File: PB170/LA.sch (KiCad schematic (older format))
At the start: 0 parts

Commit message: 11-02-2021 02 Martin
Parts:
- added U? (x3): 74HC08, Housings_SOIC:SOIC-14_3.9x8.7mm_Pitch1.27mm, symbol PB170:74HC08
- added U? (x3): 74HC32, Housings_SOIC:SOIC-14_3.9x8.7mm_Pitch1.27mm, symbol PB170:74HC32
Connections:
- new net: U?.3 (1Y), U?.4 (2A)
- new net: U?.3 (1Y), U?.9 (3A)
- new net: U?.5 (2B), U?.6 (2Y)
- new net: U?.10 (3B), U?.8 (3Y)
- new net: U?.6 (2Y), U?.9 (3A)
- new net LA: U?.8 (3Y)
- new net Q0: U?.1 (1A)
- new net Q2: U?.4 (2A)
- new net Q3: U?.1 (1A)
- new net Q4: U?.2 (1B)
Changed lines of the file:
@@
 Comment4 ""
 $EndDescr
+$Comp
+L PB170:74HC08 U?
+U 1 1 6025D3F6
+P 1450 1000
+F 0 "U?" H 1475 1267 50  0000 C CNN
+F 1 "74HC08" H 1475 1176 50  0000 C CNN
+F 2 "Housings_SOIC:SOIC-14_3.9x8.7mm_Pitch1.27mm" H 1450 1000 50  0001 C CNN
+F 3 "https://datasheet.lcsc.com/szlcsc/Nexperia-74HC08D-653_C5593.pdf" H 1450 1000 50  0001 C CNN
+F 4 "C5593" H 1450 1000 50  0001 C CNN "LCSC"
+	1    1450 1000
+	1    0    0    -1
+$EndComp
+$Comp
+L PB170:74HC08 U?
+U 2 1 6025D87D
+P 1450 1500
+F 0 "U?" H 1475 1767 50  0000 C CNN
+F 1 "74HC08" H 1475 1676 50  0000 C CNN
+F 2 "Housings_SOIC:SOIC-14_3.9x8.7mm_Pitch1.27mm" H 1450 1500 50  0001 C CNN
+F 3 "https://datasheet.lcsc.com/szlcsc/Nexperia-74HC08D-653_C5593.pdf" H 1450 1500 50  0001 C CNN
+F 4 "C5593" H 1450 1500 50  0001 C CNN "LCSC"
+	2    1450 1500
+	1    0    0    -1
+$EndComp
+$Comp
+L PB170:74HC08 U?
+U 3 1 6025DDC8
+P 2400 1950
+F 0 "U?" H 2425 2217 50  0000 C CNN
+F 1 "74HC08" H 2425 2126 50  0000 C CNN
+F 2 "Housings_SOIC:SOIC-14_3.9x8.7mm_Pitch1.27mm" H 2400 1950 50  0001 C CNN
+F 3 "https://datasheet.lcsc.com/szlcsc/Nexperia-74HC08D-653_C5593.pdf" H 2400 1950 50  0001 C CNN
+F 4 "C5593" H 2400 1950 50  0001 C CNN "LCSC"
+	3    2400 1950
+	1    0    0    -1
+$EndComp
+$Comp
+L PB170:74HC32 U?
+U 1 1 6025D4D4
+P 1500 1900
+F 0 "U?" H 1475 2175 50  0000 C CNN
+F 1 "74HC32" H 1475 2084 50  0000 C CNN
+F 2 "Housings_SOIC:SOIC-14_3.9x8.7mm_Pitch1.27mm" H 950 2100 50  0001 C CNN
+F 3 "https://datasheet.lcsc.com/szlcsc/Nexperia-74HC32D-653_C5632.pdf" H 950 2100 50  0001 C CNN
+F 4 "C5632" H 1500 1900 50  0001 C CNN "LCSC"
+	1    1500 1900
+	1    0    0    -1
+$EndComp
+$Comp
+L PB170:74HC32 U?
+U 2 1 6025E621
+P 2450 1200
+F 0 "U?" H 2425 1475 50  0000 C CNN
+F 1 "74HC32" H 2425 1384 50  0000 C CNN
+F 2 "Housings_SOIC:SOIC-14_3.9x8.7mm_Pitch1.27mm" H 1900 1400 50  0001 C CNN
+F 3 "https://datasheet.lcsc.com/szlcsc/Nexperia-74HC32D-653_C5632.pdf" H 1900 1400 50  0001 C CNN
+F 4 "C5632" H 2450 1200 50  0001 C CNN "LCSC"
+	2    2450 1200
+	1    0    0    -1
+$EndComp
+$Comp
+L PB170:74HC32 U?
+U 3 1 6025FAD0
+P 3050 1500
+F 0 "U?" H 3025 1775 50  0000 C CNN
+F 1 "74HC32" H 3025 1684 50  0000 C CNN
+F 2 "Housings_SOIC:SOIC-14_3.9x8.7mm_Pitch1.27mm" H 2500 1700 50  0001 C CNN
+F 3 "https://datasheet.lcsc.com/szlcsc/Nexperia-74HC32D-653_C5632.pdf" H 2500 1700 50  0001 C CNN
+F 4 "C5632" H 3050 1500 50  0001 C CNN "LCSC"
+	3    3050 1500
+	1    0    0    -1
+$EndComp
+Wire Wire Line
+	1750 1000 2050 1000
+Wire Wire Line
+	2050 1000 2050 1150
+Wire Wire Line
+	2050 1150 2200 1150
+Wire Wire Line
+	1750 1500 2050 1500
+Wire Wire Line
+	2050 1500 2050 1250
+Wire Wire Line
+	2050 1250 2200 1250
+Wire Wire Line
+	1700 1900 2150 1900
+Wire Wire Line
+	2700 1950 2750 1950
+Wire Wire Line
+	2750 1950 2750 1550
+Wire Wire Line
+	2750 1550 2800 1550
+Wire Wire Line
+	2800 1450 2750 1450
+Wire Wire Line
+	2750 1450 2750 1200
+Wire Wire Line
+	2750 1200 2650 1200
+Text GLabel 1200 950  0    50   Input ~ 0
+Q0
+Text GLabel 1250 1850 0    50   Input ~ 0
+Q3
+Text GLabel 1200 1450 0    50   Input ~ 0
+Q2
+Text GLabel 1250 1950 0    50   Input ~ 0
+Q4
+Text GLabel 3250 1500 2    50   Output ~ 0
+LA
 $EndSCHEMATC

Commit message: LA changed
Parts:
- added U?: 74HC00, Package_SO:TSSOP-14_4.4x5mm_P0.65mm, symbol 74xx:74HC00
- U? (x2): value 74HC08 -> 74HC00; footprint Housings_SOIC:SOIC-14_3.9x8.7mm_Pitch1.27mm -> Package_SO:TSSOP-14_4.4x5mm_P0.65mm
- U? (x2): value 74HC32 -> 74HC00; footprint Housings_SOIC:SOIC-14_3.9x8.7mm_Pitch1.27mm -> Package_SO:TSSOP-14_4.4x5mm_P0.65mm
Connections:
- net at U?.2 (1B): now also U?.3
- net 11: now reaches U?.5 (2B)
- net 11: now also U?.1, U?.2
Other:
- moved on the sheet: U?A, U?B, U?C
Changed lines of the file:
@@
 L PB170:74HC08 U?
 U 1 1 6025D3F6
-P 1450 1000
-F 0 "U?" H 1475 1267 50  0000 C CNN
-F 1 "74HC08" H 1475 1176 50  0000 C CNN
-F 2 "Housings_SOIC:SOIC-14_3.9x8.7mm_Pitch1.27mm" H 1450 1000 50  0001 C CNN
-F 3 "https://datasheet.lcsc.com/szlcsc/Nexperia-74HC08D-653_C5593.pdf" H 1450 1000 50  0001 C CNN
-F 4 "C5593" H 1450 1000 50  0001 C CNN "LCSC"
-	1    1450 1000
+P 5200 3300
+F 0 "U?" H 5225 3567 50  0000 C CNN
+F 1 "74HC08" H 5225 3476 50  0000 C CNN
+F 2 "Housings_SOIC:SOIC-14_3.9x8.7mm_Pitch1.27mm" H 5200 3300 50  0001 C CNN
+F 3 "https://datasheet.lcsc.com/szlcsc/Nexperia-74HC08D-653_C5593.pdf" H 5200 3300 50  0001 C CNN
+F 4 "C5593" H 5200 3300 50  0001 C CNN "LCSC"
+	1    5200 3300
 	1    0    0    -1
 $EndComp
@@
 L PB170:74HC08 U?
 U 2 1 6025D87D
-P 1450 1500
-F 0 "U?" H 1475 1767 50  0000 C CNN
-F 1 "74HC08" H 1475 1676 50  0000 C CNN
-F 2 "Housings_SOIC:SOIC-14_3.9x8.7mm_Pitch1.27mm" H 1450 1500 50  0001 C CNN
-F 3 "https://datasheet.lcsc.com/szlcsc/Nexperia-74HC08D-653_C5593.pdf" H 1450 1500 50  0001 C CNN
-F 4 "C5593" H 1450 1500 50  0001 C CNN "LCSC"
-	2    1450 1500
+P 5200 3800
+F 0 "U?" H 5225 4067 50  0000 C CNN
+F 1 "74HC00" H 5225 3976 50  0000 C CNN
+F 2 "Package_SO:TSSOP-14_4.4x5mm_P0.65mm" H 5200 3800 50  0001 C CNN
+F 3 "https://datasheet.lcsc.com/szlcsc/Texas-Instruments-TI-SN74HC00PWR_C6807.pdf" H 5200 3800 50  0001 C CNN
+F 4 "C5593" H 5200 3800 50  0001 C CNN "LCSC"
+	2    5200 3800
 	1    0    0    -1
 $EndComp
@@
 L PB170:74HC08 U?
 U 3 1 6025DDC8
-P 2400 1950
-F 0 "U?" H 2425 2217 50  0000 C CNN
-F 1 "74HC08" H 2425 2126 50  0000 C CNN
-F 2 "Housings_SOIC:SOIC-14_3.9x8.7mm_Pitch1.27mm" H 2400 1950 50  0001 C CNN
-F 3 "https://datasheet.lcsc.com/szlcsc/Nexperia-74HC08D-653_C5593.pdf" H 2400 1950 50  0001 C CNN
-F 4 "C5593" H 2400 1950 50  0001 C CNN "LCSC"
-	3    2400 1950
+P 6150 4250
+F 0 "U?" H 6175 4517 50  0000 C CNN
+F 1 "74HC00" H 6175 4426 50  0000 C CNN
+F 2 "Package_SO:TSSOP-14_4.4x5mm_P0.65mm" H 6150 4250 50  0001 C CNN
+F 3 "https://datasheet.lcsc.com/szlcsc/Texas-Instruments-TI-SN74HC00PWR_C6807.pdf" H 6150 4250 50  0001 C CNN
+F 4 "C5593" H 6150 4250 50  0001 C CNN "LCSC"
+	3    6150 4250
 	1    0    0    -1
 $EndComp
@@
 L PB170:74HC32 U?
 U 1 1 6025D4D4
-P 1500 1900
-F 0 "U?" H 1475 2175 50  0000 C CNN
-F 1 "74HC32" H 1475 2084 50  0000 C CNN
-F 2 "Housings_SOIC:SOIC-14_3.9x8.7mm_Pitch1.27mm" H 950 2100 50  0001 C CNN
-F 3 "https://datasheet.lcsc.com/szlcsc/Nexperia-74HC32D-653_C5632.pdf" H 950 2100 50  0001 C CNN
-F 4 "C5632" H 1500 1900 50  0001 C CNN "LCSC"
-	1    1500 1900
+P 5250 4200
+F 0 "U?" H 5225 4475 50  0000 C CNN
+F 1 "74HC32" H 5225 4384 50  0000 C CNN
+F 2 "Housings_SOIC:SOIC-14_3.9x8.7mm_Pitch1.27mm" H 4700 4400 50  0001 C CNN
+F 3 "https://datasheet.lcsc.com/szlcsc/Nexperia-74HC32D-653_C5632.pdf" H 4700 4400 50  0001 C CNN
+F 4 "C5632" H 5250 4200 50  0001 C CNN "LCSC"
+	1    5250 4200
 	1    0    0    -1
 $EndComp
@@
 L PB170:74HC32 U?
 U 2 1 6025E621
-P 2450 1200
-F 0 "U?" H 2425 1475 50  0000 C CNN
-F 1 "74HC32" H 2425 1384 50  0000 C CNN
-F 2 "Housings_SOIC:SOIC-14_3.9x8.7mm_Pitch1.27mm" H 1900 1400 50  0001 C CNN
-F 3 "https://datasheet.lcsc.com/szlcsc/Nexperia-74HC32D-653_C5632.pdf" H 1900 1400 50  0001 C CNN
-F 4 "C5632" H 2450 1200 50  0001 C CNN "LCSC"
-	2    2450 1200
+P 6200 3500
+F 0 "U?" H 6175 3775 50  0000 C CNN
+F 1 "74HC00" H 6175 3684 50  0000 C CNN
+F 2 "Package_SO:TSSOP-14_4.4x5mm_P0.65mm" H 5650 3700 50  0001 C CNN
+F 3 "https://datasheet.lcsc.com/szlcsc/Texas-Instruments-TI-SN74HC00PWR_C6807.pdf" H 5650 3700 50  0001 C CNN
+F 4 "C5632" H 6200 3500 50  0001 C CNN "LCSC"
+	2    6200 3500
 	1    0    0    -1
 $EndComp
@@
 L PB170:74HC32 U?
 U 3 1 6025FAD0
-P 3050 1500
-F 0 "U?" H 3025 1775 50  0000 C CNN
-F 1 "74HC32" H 3025 1684 50  0000 C CNN
-F 2 "Housings_SOIC:SOIC-14_3.9x8.7mm_Pitch1.27mm" H 2500 1700 50  0001 C CNN
-F 3 "https://datasheet.lcsc.com/szlcsc/Nexperia-74HC32D-653_C5632.pdf" H 2500 1700 50  0001 C CNN
-F 4 "C5632" H 3050 1500 50  0001 C CNN "LCSC"
-	3    3050 1500
+P 6800 3800
+F 0 "U?" H 6775 4075 50  0000 C CNN
+F 1 "74HC00" H 6775 3984 50  0000 C CNN
+F 2 "Package_SO:TSSOP-14_4.4x5mm_P0.65mm" H 6250 4000 50  0001 C CNN
+F 3 "https://datasheet.lcsc.com/szlcsc/Texas-Instruments-TI-SN74HC00PWR_C6807.pdf" H 6250 4000 50  0001 C CNN
+F 4 "C5632" H 6800 3800 50  0001 C CNN "LCSC"
+	3    6800 3800
 	1    0    0    -1
 $EndComp
 Wire Wire Line
-	1750 1000 2050 1000
+	5500 3300 5800 3300
 Wire Wire Line
-	2050 1000 2050 1150
+	5800 3300 5800 3450
 Wire Wire Line
-	2050 1150 2200 1150
+	5800 3450 5950 3450
 Wire Wire Line
-	1750 1500 2050 1500
+	5500 3800 5800 3800
 Wire Wire Line
-	2050 1500 2050 1250
+	5800 3800 5800 3550
 Wire Wire Line
-	2050 1250 2200 1250
+	5800 3550 5950 3550
 Wire Wire Line
-	1700 1900 2150 1900
+	5450 4200 5900 4200
 Wire Wire Line
-	2700 1950 2750 1950
+	6450 4250 6500 4250
 Wire Wire Line
-	2750 1950 2750 1550
+	6500 4250 6500 3850
 Wire Wire Line
-	2750 1550 2800 1550
+	6500 3850 6550 3850
 Wire Wire Line
-	2800 1450 2750 1450
+	6550 3750 6500 3750
 Wire Wire Line
-	2750 1450 2750 1200
+	6500 3750 6500 3500
 Wire Wire Line
-	2750 1200 2650 1200
-Text GLabel 1200 950  0    50   Input ~ 0
+	6500 3500 6400 3500
+Text GLabel 4950 3250 0    50   Input ~ 0
 Q0
-Text GLabel 1250 1850 0    50   Input ~ 0
+Text GLabel 5000 4150 0    50   Input ~ 0
 Q3
-Text GLabel 1200 1450 0    50   Input ~ 0
+Text GLabel 4950 3750 0    50   Input ~ 0
 Q2
-Text GLabel 1250 1950 0    50   Input ~ 0
+Text GLabel 5000 4250 0    50   Input ~ 0
 Q4
-Text GLabel 3250 1500 2    50   Output ~ 0
+Text GLabel 7000 3800 2    50   Output ~ 0
 LA
+$Comp
+L 74xx:74HC00 U?
+U 1 1 6027EE26
+P 4400 3350
+F 0 "U?" H 4400 3675 50  0000 C CNN
+F 1 "74HC00" H 4400 3584 50  0000 C CNN
+F 2 "Package_SO:TSSOP-14_4.4x5mm_P0.65mm" H 4400 3350 50  0001 C CNN
+F 3 "https://datasheet.lcsc.com/szlcsc/Texas-Instruments-TI-SN74HC00PWR_C6807.pdf" H 4400 3350 50  0001 C CNN
+F 4 "C6807" H 4400 3350 50  0001 C CNN "LCSC"
+	1    4400 3350
+	1    0    0    -1
+$EndComp
+Wire Wire Line
+	4950 3350 4700 3350
+Wire Wire Line
+	4100 3250 4000 3250
+Wire Wire Line
+	4000 3250 4000 3350
+Wire Wire Line
+	4000 3450 4100 3450
+Wire Wire Line
+	4000 3350 3900 3350
+Connection ~ 4000 3350
+Wire Wire Line
+	4000 3350 4000 3450
+Text GLabel 3900 3350 0    50   Input ~ 0
+11
+Wire Wire Line
+	4000 3450 4000 3850
+Wire Wire Line
+	4000 3850 4950 3850
+Connection ~ 4000 3450
 $EndSCHEMATC

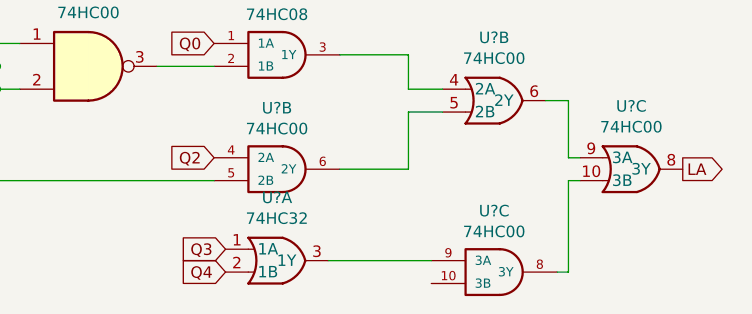
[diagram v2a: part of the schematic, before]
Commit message: added some labels
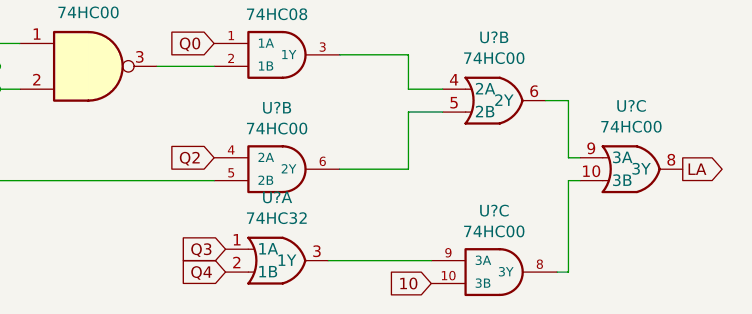
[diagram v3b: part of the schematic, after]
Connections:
- net 10: now reaches U?.10 (3B)
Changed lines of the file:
@@
 $Descr A4 11693 8268
 encoding utf-8
-Sheet 3 7
+Sheet 3 6
 Title ""
 Date ""
@@
 	4000 3850 4950 3850
 Connection ~ 4000 3450
+Text GLabel 5900 4300 0    50   Input ~ 0
+10
 $EndSCHEMATC
